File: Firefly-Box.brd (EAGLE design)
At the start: 90 x 56 mm, 35 parts, among them J1 USB MICRO, U1 ATMEGA32U4-XUMU, U2 ATMEGA32U4-XUAU, Y1 16MHz KX-7

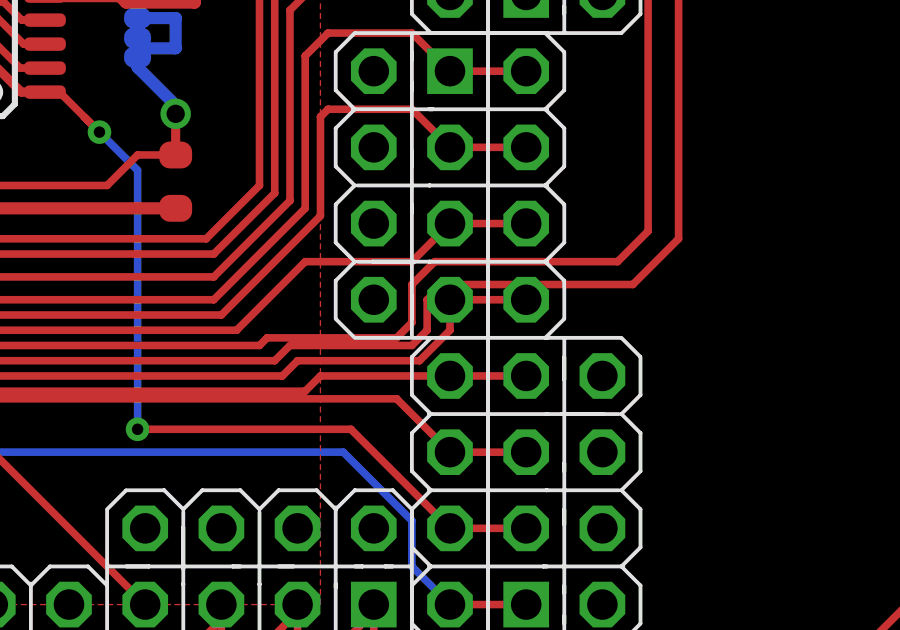
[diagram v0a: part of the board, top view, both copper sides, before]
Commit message: Fixed pin names
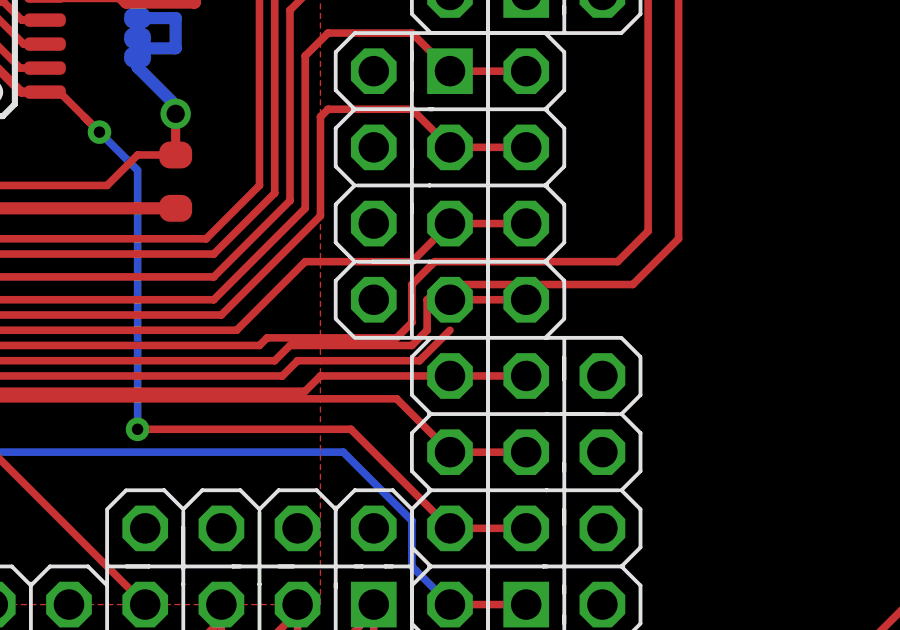
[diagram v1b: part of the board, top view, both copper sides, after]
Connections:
- net A0 renamed D10/A0
- net A1 renamed D9/A1
- net A2 renamed D8/A2
- net A3 renamed D7/A3
- net A4 renamed D6/A4
- net A5 renamed D5/A5
- net D5* renamed D3*
- net D6* renamed D13*
- net IO10* renamed D11*
- net IO11* renamed D2*
- net IO13* renamed D4*
- net IO8 renamed D15
- net IO9* renamed D12*
- removed net D4: BUS1.3, U1.25, U2.25
- removed net N$25: BUS3.4
- removed net N$26: BUS3.5
- removed net N$33: BUS4.4
- removed net N$34: BUS4.5
- removed net N$48: BUS2.4
- removed net NC: BUS1.5
- removed net NC2: BUS1.4
- removed net NC3: BUS2.5
- new net D14: AH1.6, AH2.1, U1.1, U2.1
- net SPI-CS1: now also BUS1.3, U1.25, U2.25; no longer BUS3.3, U1.8, U2.8
- net SPI-CS2: now also BUS2.3, U1.26, U2.26; no longer AH1.6, AH2.1, U1.1, U2.1
- net SPI-CS3: now also BUS3.3, U1.8, U2.8; no longer BUS2.3, U1.26, U2.26
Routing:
- net D4: track 36.0 -> 0.00 mm
- net D14: track 0.00 -> 31.0 mm, vias 0 -> 2
- net SPI-CS2: track 31.0 -> 49.5 mm, vias 2 -> 0
- net SPI-CS1: track 45.9 -> 36.0 mm, vias 1 -> 0
- net SPI-CS3: track 49.5 -> 45.9 mm, vias 0 -> 1
- net D11*: track 53.7 -> 52.7 mm
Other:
- board text added: "TODO: 3.3V Power Supply"
- board text added: "TODO: MINI USB"
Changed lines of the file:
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@@
 <setting verticaltext="up"/>
 </settings>
-<grid distance="10" unitdist="mil" unit="mil" style="lines" multiple="1" display="yes" altdistance="1" altunitdist="mil" altunit="mil"/>
+<grid distance="0.05" unitdist="inch" unit="inch" style="lines" multiple="1" display="yes" altdistance="0.005" altunitdist="inch" altunit="inch"/>
 <layers>
 <layer number="1" name="Top" color="4" fill="1" visible="yes" active="yes"/>
@@
 <layer number="46" name="Milling" color="3" fill="1" visible="no" active="yes"/>
 <layer number="47" name="Measures" color="7" fill="1" visible="no" active="yes"/>
-<layer number="48" name="Document" color="7" fill="1" visible="no" active="yes"/>
+<layer number="48" name="Document" color="7" fill="1" visible="yes" active="yes"/>
 <layer number="49" name="Reference" color="7" fill="1" visible="no" active="yes"/>
 <layer number="50" name="dxf" color="7" fill="1" visible="no" active="yes"/>
@@
 <board>
 <plain>
+<text x="2.54" y="63.5" size="1.778" layer="48" font="vector" ratio="15">TODO: 3.3V Power Supply</text>
+<text x="2.54" y="60.96" size="1.778" layer="48" font="vector" ratio="15">TODO: MINI USB</text>
 </plain>
 <attributes>
@@
 <wire x1="3.81" y1="12.304" x2="5.588" y2="8.89" width="0" layer="19" extent="1-1"/>
 </signal>
-<signal name="SPI-CS3">
+<signal name="SPI-CS2">
 <contactref element="U1" pad="26"/>
 <contactref element="U2" pad="26"/>
@@
 <wire x1="46.228" y1="44.45" x2="43.688" y2="44.45" width="0.254" layer="1"/>
 </signal>
-<signal name="IO11*">
+<signal name="D2*">
 <contactref element="U1" pad="12"/>
 <contactref element="U2" pad="12"/>
@@
 <wire x1="42.418" y1="37.338" x2="42.418" y2="40.64" width="0.254" layer="1"/>
 </signal>
-<signal name="IO9*">
+<signal name="D12*">
 <contactref element="U1" pad="29"/>
 <contactref element="U2" pad="29"/>
@@
 <wire x1="43.688" y1="16.51" x2="46.228" y2="16.51" width="0.254" layer="1"/>
 </signal>
-<signal name="IO10*">
-<contactref element="U1" pad="30"/>
-<contactref element="U2" pad="30"/>
-<wire x1="19.9042" y1="28.972" x2="21.109" y2="28.972" width="0.254" layer="1"/>
-<wire x1="18.584" y1="28.372" x2="19.3042" y2="28.372" width="0.254" layer="1"/>
-<wire x1="19.3042" y1="28.372" x2="19.9042" y2="28.972" width="0.254" layer="1"/>
-<contactref element="AH1" pad="3"/>
-<contactref element="AH2" pad="4"/>
-<wire x1="43.688" y1="19.05" x2="43.688" y2="18.034" width="0.254" layer="1"/>
-<wire x1="43.688" y1="18.034" x2="42.672" y2="17.018" width="0.254" layer="1"/>
-<wire x1="42.672" y1="17.018" x2="38.608" y2="17.018" width="0.254" layer="1"/>
-<wire x1="38.608" y1="17.018" x2="38.1" y2="16.51" width="0.254" layer="1"/>
-<wire x1="38.1" y1="16.51" x2="23.622" y2="16.51" width="0.254" layer="1"/>
-<wire x1="23.622" y1="16.51" x2="21.082" y2="19.05" width="0.254" layer="1"/>
-<wire x1="21.082" y1="19.05" x2="15.24" y2="19.05" width="0.254" layer="1"/>
-<wire x1="15.24" y1="19.05" x2="10.922" y2="23.368" width="0.254" layer="1"/>
-<wire x1="10.922" y1="23.368" x2="10.922" y2="25.654" width="0.254" layer="1"/>
-<wire x1="10.922" y1="25.654" x2="13.716" y2="28.448" width="0.254" layer="1"/>
-<wire x1="18.584" y1="28.372" x2="13.792" y2="28.372" width="0.254" layer="1"/>
-<wire x1="13.792" y1="28.372" x2="13.716" y2="28.448" width="0.254" layer="1"/>
-<wire x1="43.688" y1="19.05" x2="46.228" y2="19.05" width="0.254" layer="1"/>
-</signal>
-<signal name="A3">
+<signal name="D7/A3">
 <contactref element="U1" pad="39"/>
 <contactref element="U2" pad="39"/>
@@
 <wire x1="43.688" y1="29.21" x2="46.228" y2="29.21" width="0.254" layer="1"/>
 </signal>
-<signal name="A2">
+<signal name="D8/A2">
 <contactref element="U1" pad="38"/>
 <contactref element="U2" pad="38"/>
@@
 <wire x1="43.688" y1="26.67" x2="46.228" y2="26.67" width="0.254" layer="1"/>
 </signal>
-<signal name="A1">
+<signal name="D9/A1">
 <contactref element="U1" pad="37"/>
 <contactref element="U2" pad="37"/>
@@
 <wire x1="43.688" y1="24.13" x2="46.228" y2="24.13" width="0.254" layer="1"/>
 </signal>
-<signal name="A0">
+<signal name="D10/A0">
 <contactref element="U1" pad="36"/>
 <contactref element="U2" pad="36"/>
@@
 <wire x1="43.688" y1="21.59" x2="46.228" y2="21.59" width="0.254" layer="1"/>
 </signal>
-<signal name="A4">
+<signal name="D6/A4">
 <contactref element="U1" pad="40"/>
 <contactref element="U2" pad="40"/>
@@
 <wire x1="43.688" y1="31.75" x2="46.228" y2="31.75" width="0.254" layer="1"/>
 </signal>
-<signal name="A5">
+<signal name="D5/A5">
 <contactref element="U1" pad="41"/>
 <contactref element="U2" pad="41"/>
@@
 <wire x1="43.688" y1="34.29" x2="46.228" y2="34.29" width="0.254" layer="1"/>
 </signal>
-<signal name="D5*">
+<signal name="D3*">
 <contactref element="U2" pad="31"/>
 <contactref element="U1" pad="31"/>
@@
 <wire x1="34.544" y1="23.876" x2="33.274" y2="23.876" width="0.254" layer="1"/>
 </signal>
-<signal name="SPI-CS1">
+<signal name="SPI-CS3">
 <contactref element="U1" pad="8"/>
 <contactref element="U2" pad="8"/>
@@
 <wire x1="33.198" y1="31.572" x2="33.274" y2="31.496" width="0.254" layer="1"/>
 </signal>
-<signal name="D6*">
+<signal name="D13*">
 <contactref element="U1" pad="27"/>
 <contactref element="U2" pad="27"/>
@@
 <wire x1="43.688" y1="13.97" x2="46.228" y2="13.97" width="0.254" layer="1"/>
 </signal>
-<signal name="IO13*">
+<signal name="D4*">
 <contactref element="U2" pad="32"/>
 <contactref element="U1" pad="32"/>
@@
 <wire x1="5.604" y1="17.018" x2="12.192" y2="24.13" width="0" layer="19" extent="1-1"/>
 </signal>
-<signal name="IO8">
+<signal name="D15">
 <contactref element="U1" pad="28"/>
 <contactref element="U2" pad="28"/>
@@
 <wire x1="43.688" y1="8.89" x2="46.228" y2="8.89" width="0.254" layer="1"/>
 </signal>
-<signal name="SPI-CS2">
+<signal name="D14">
 <contactref element="U1" pad="1"/>
 <contactref element="U2" pad="1"/>
@@
 <wire x1="18.52" y1="25.908" x2="18.584" y2="25.972" width="0.254" layer="1"/>
 </signal>
-<signal name="D4">
+<signal name="SPI-CS1">
 <contactref element="U2" pad="25"/>
 <contactref element="U1" pad="25"/>
@@
 <wire x1="20.384" y1="35.772" x2="20.384" y2="51.118" width="0.254" layer="1"/>
 <wire x1="21.884" y1="33.247" x2="20.384" y2="35.772" width="0" layer="19" extent="1-1"/>
-</signal>
-<signal name="N$25">
-<contactref element="BUS3" pad="4"/>
-</signal>
-<signal name="N$26">
-<contactref element="BUS3" pad="5"/>
-</signal>
-<signal name="N$33">
-<contactref element="BUS4" pad="4"/>
-</signal>
-<signal name="N$34">
-<contactref element="BUS4" pad="5"/>
-</signal>
-<signal name="N$48">
-<contactref element="BUS2" pad="4"/>
-</signal>
-<signal name="NC">
-<contactref element="BUS1" pad="5"/>
-</signal>
-<signal name="NC2">
-<contactref element="BUS1" pad="4"/>
 </signal>
 <signal name="3V3">
@@
 <wire x1="2.286" y1="13.604" x2="3.81" y2="13.604" width="0" layer="19" extent="1-1"/>
 </signal>
-<signal name="NC3">
-<contactref element="BUS2" pad="5"/>
+<signal name="D11*">
+<contactref element="AH1" pad="3"/>
+<contactref element="AH2" pad="4"/>
+<wire x1="43.688" y1="19.05" x2="46.228" y2="19.05" width="0.254" layer="1"/>
+<contactref element="U1" pad="30"/>
+<contactref element="U2" pad="30"/>
+<wire x1="19.9042" y1="28.972" x2="21.109" y2="28.972" width="0.254" layer="1"/>
+<wire x1="18.584" y1="28.372" x2="19.3042" y2="28.372" width="0.254" layer="1"/>
+<wire x1="19.3042" y1="28.372" x2="19.9042" y2="28.972" width="0.254" layer="1"/>
+<wire x1="43.688" y1="18.034" x2="42.672" y2="17.018" width="0.254" layer="1"/>
+<wire x1="42.672" y1="17.018" x2="38.608" y2="17.018" width="0.254" layer="1"/>
+<wire x1="38.608" y1="17.018" x2="38.1" y2="16.51" width="0.254" layer="1"/>
+<wire x1="38.1" y1="16.51" x2="23.622" y2="16.51" width="0.254" layer="1"/>
+<wire x1="23.622" y1="16.51" x2="21.082" y2="19.05" width="0.254" layer="1"/>
+<wire x1="21.082" y1="19.05" x2="15.24" y2="19.05" width="0.254" layer="1"/>
+<wire x1="15.24" y1="19.05" x2="10.922" y2="23.368" width="0.254" layer="1"/>
+<wire x1="10.922" y1="23.368" x2="10.922" y2="25.654" width="0.254" layer="1"/>
+<wire x1="10.922" y1="25.654" x2="13.716" y2="28.448" width="0.254" layer="1"/>
+<wire x1="18.584" y1="28.372" x2="13.792" y2="28.372" width="0.254" layer="1"/>
+<wire x1="13.792" y1="28.372" x2="13.716" y2="28.448" width="0.254" layer="1"/>
+<wire x1="43.688" y1="18.034" x2="43.688" y2="19.05" width="0" layer="19" extent="1-1"/>
 </signal>
 </signals>

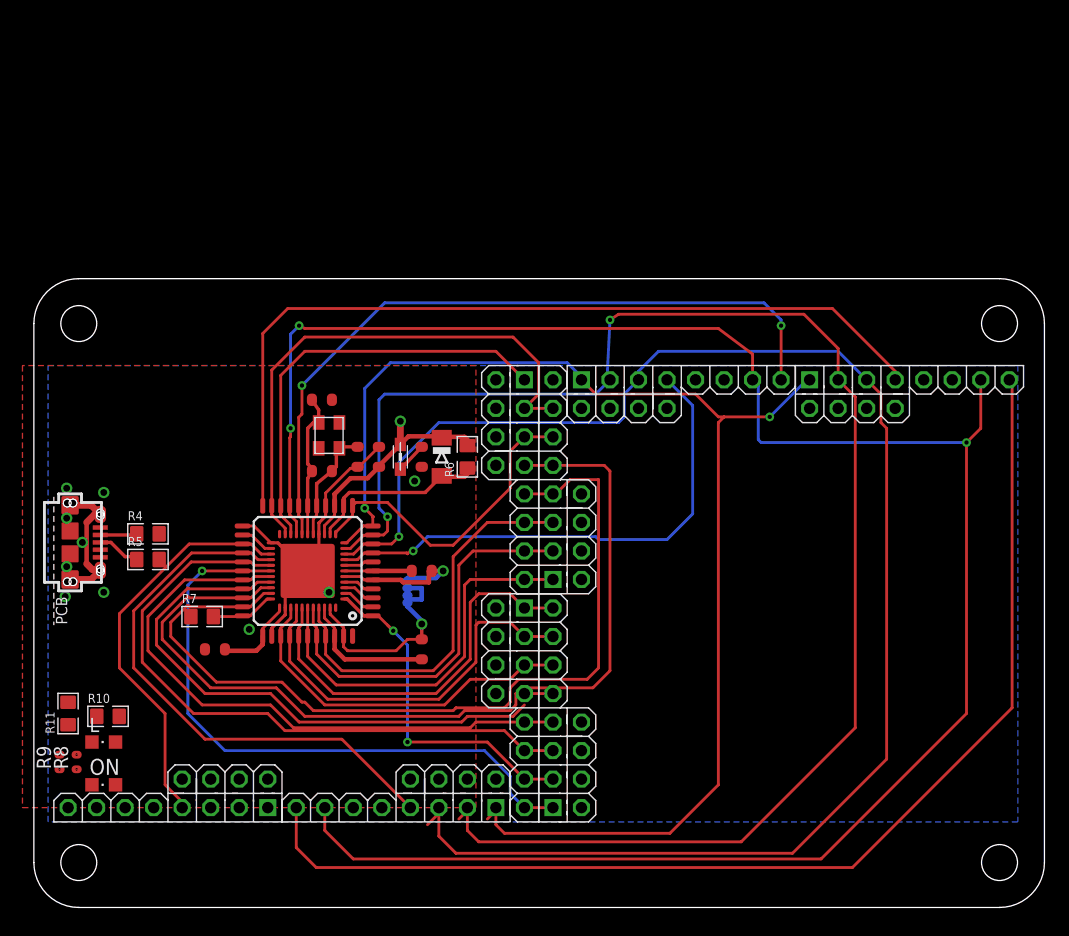
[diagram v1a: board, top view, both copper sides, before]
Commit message: Add Box headers
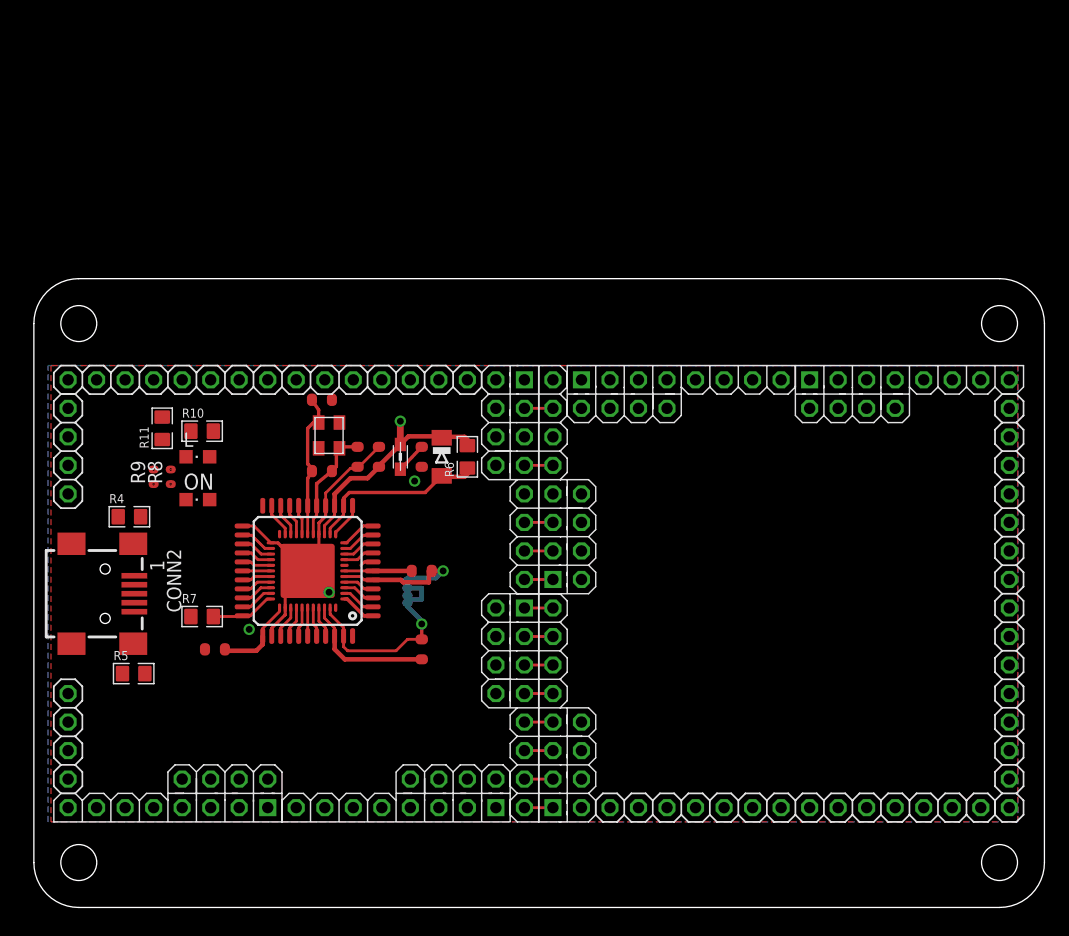
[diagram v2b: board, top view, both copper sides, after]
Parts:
- removed J1: USB MICRO, SmartPrj:CON2_USB_MICRO_B_AT
- added CONN2: CONN_USB, dp_devices:CONN_USB_MINI-B
- added JP1, JP2: (no value), pinhead:1X15
- added JP3: (no value), pinhead:1X14
- added JP4, JP5: (no value), pinhead:1X04
- moved ON 26.7 mm to (14.6, 36.3)
- moved L 26.7 mm to (14.6, 40.1)
- moved R10 26.7 mm to (15.0, 42.4)
- moved R11 26.7 mm to (11.4, 42.7)
- moved R8 26.7 mm to (12.2, 38.4)
- moved R9 26.7 mm to (10.7, 38.4)
- moved R5 10.2 mm to (8.89, 20.8)
- moved R4 2.25 mm to (8.51, 34.8)
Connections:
- removed net USBID: J1.P4
- removed net XUSB: J1.P1
- new net 5V: CONN2.VUSB, U1.7
- net D+: now also CONN2.D+; no longer J1.P3
- net D-: now also CONN2.D-; no longer J1.P2
- net GND: now also CONN2.GND; no longer J1.P5, J1.S1, J1.S2, J1.S3, J1.S4, J1.S5, J1.S6
- net VUSB: no longer U1.7
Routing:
- net I2C-SDA: track 182.7 -> 2.77 mm, vias 3 -> 0
- net I2C-SCL: track 168.4 -> 2.65 mm, vias 2 -> 0
- net SPI-SCK: track 143.8 -> 2.90 mm, vias 1 -> 0
- net SPI-MOSI: track 142.2 -> 3.01 mm, vias 2 -> 0
- net SPI-MISO: track 117.6 -> 3.15 mm, vias 2 -> 0
- net D3*: track 83.2 -> 5.44 mm
- net SPI-CS4: track 75.7 -> 0.00 mm
- net D4*: track 78.4 -> 3.02 mm
- net D13*: track 57.8 -> 5.19 mm
- net D15: track 56.2 -> 5.07 mm, vias 1 -> 0
- net D12*: track 54.6 -> 5.19 mm
- net D11*: track 52.7 -> 5.31 mm
- net SPI-CS2: track 49.5 -> 2.77 mm
- net SPI-CS3: track 45.9 -> 2.77 mm, vias 1 -> 0
- net D1/TX: track 48.2 -> 5.56 mm
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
